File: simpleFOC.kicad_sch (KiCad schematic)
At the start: 20 parts, among them M1 Conn_01x03, M2 Conn_01x03, U6 DRV8313PWP, U7 DRV8313PWP

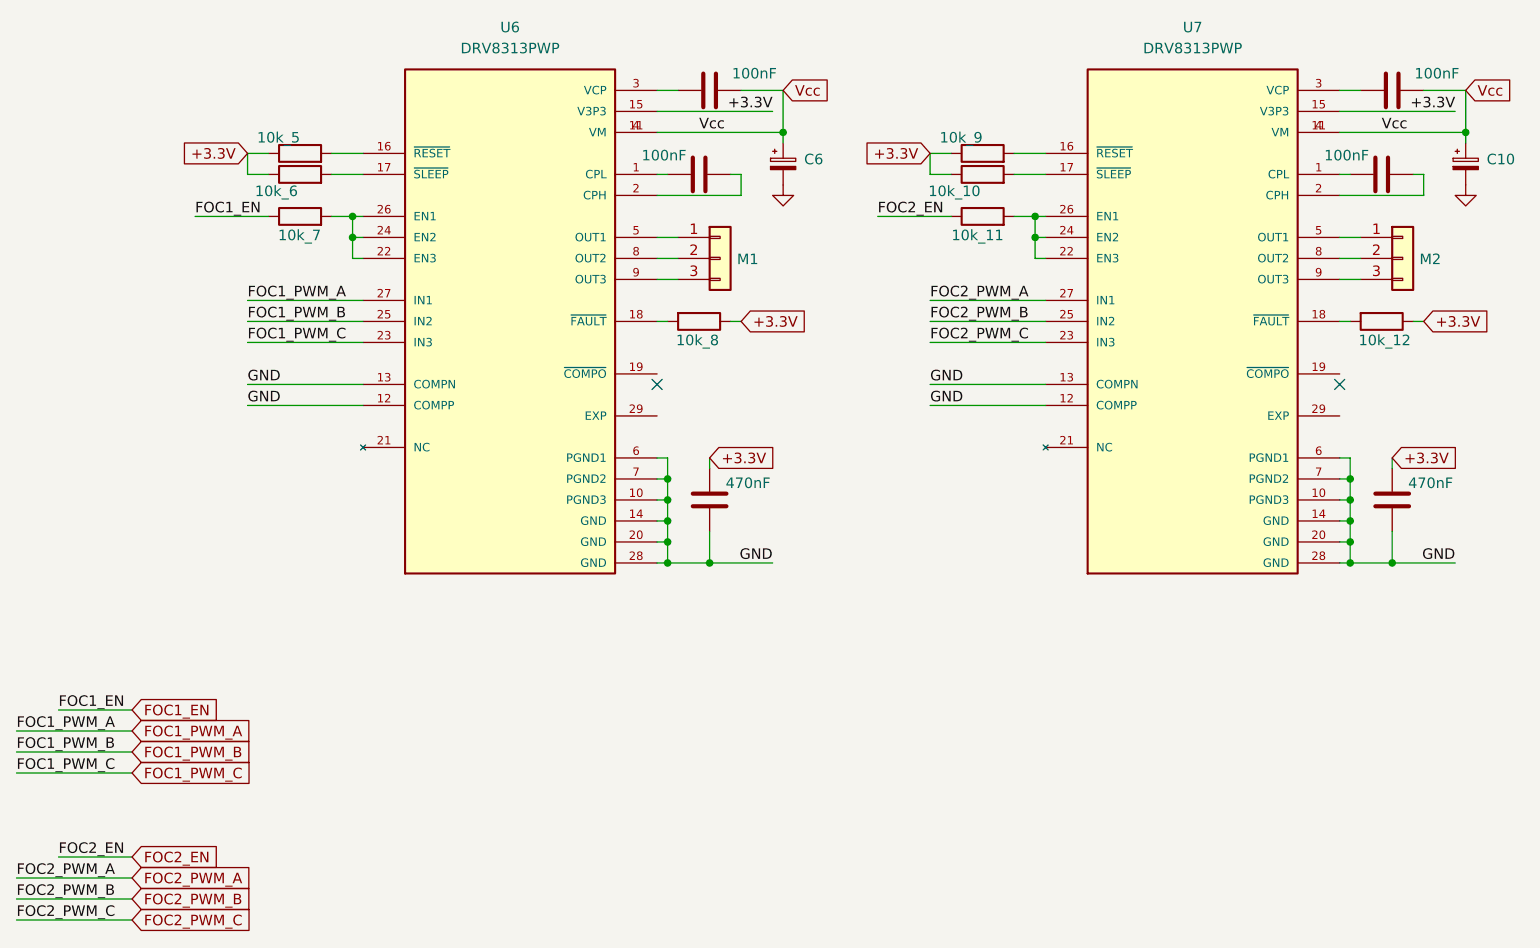
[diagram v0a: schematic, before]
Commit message: added DRV8313
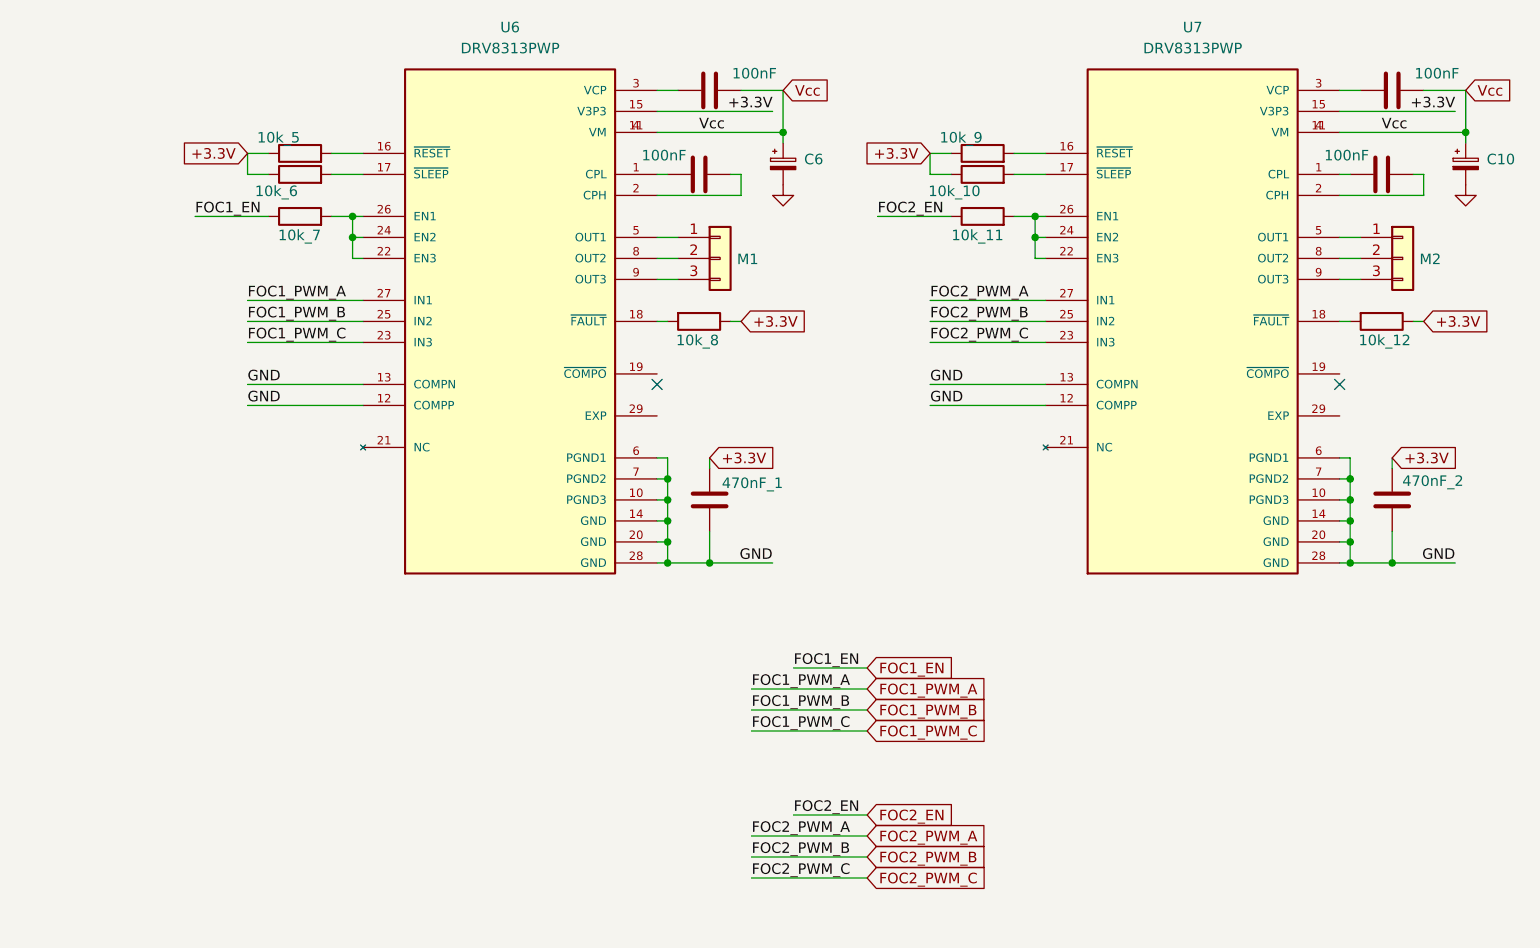
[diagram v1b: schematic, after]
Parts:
- renumbered C5 to 470nF_1, C9 to 470nF_2
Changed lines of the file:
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@@
 	(wire
 		(pts
-			(xy 33.02 154.94) (xy 46.99 154.94)
+			(xy 121.92 149.86) (xy 135.89 149.86)
 		)
 		(stroke
@@
 	(wire
 		(pts
-			(xy 38.1 167.64) (xy 46.99 167.64)
+			(xy 127 162.56) (xy 135.89 162.56)
 		)
 		(stroke
@@
 	(wire
 		(pts
-			(xy 33.02 152.4) (xy 46.99 152.4)
+			(xy 121.92 147.32) (xy 135.89 147.32)
 		)
 		(stroke
@@
 	(wire
 		(pts
-			(xy 33.02 170.18) (xy 46.99 170.18)
+			(xy 121.92 165.1) (xy 135.89 165.1)
 		)
 		(stroke
@@
 	(wire
 		(pts
-			(xy 33.02 157.48) (xy 46.99 157.48)
+			(xy 121.92 152.4) (xy 135.89 152.4)
 		)
 		(stroke
@@
 	(wire
 		(pts
-			(xy 38.1 149.86) (xy 46.99 149.86)
+			(xy 127 144.78) (xy 135.89 144.78)
 		)
 		(stroke
@@
 	(wire
 		(pts
-			(xy 33.02 175.26) (xy 46.99 175.26)
+			(xy 121.92 170.18) (xy 135.89 170.18)
 		)
 		(stroke
@@
 	(wire
 		(pts
-			(xy 33.02 172.72) (xy 46.99 172.72)
+			(xy 121.92 167.64) (xy 135.89 167.64)
 		)
 		(stroke
@@
 	)
 	(label "FOC1_PWM_B"
-		(at 33.02 154.94 0)
+		(at 121.92 149.86 0)
 		(effects
 			(font
@@
 	)
 	(label "FOC2_EN"
-		(at 38.1 167.64 0)
+		(at 127 162.56 0)
 		(effects
 			(font
@@
 	)
 	(label "FOC2_PWM_C"
-		(at 33.02 175.26 0)
+		(at 121.92 170.18 0)
 		(effects
 			(font
@@
 	)
 	(label "FOC2_PWM_A"
-		(at 33.02 170.18 0)
+		(at 121.92 165.1 0)
 		(effects
 			(font
@@
 	)
 	(label "FOC1_PWM_C"
-		(at 33.02 157.48 0)
+		(at 121.92 152.4 0)
 		(effects
 			(font
@@
 	)
 	(label "FOC2_PWM_B"
-		(at 33.02 172.72 0)
+		(at 121.92 167.64 0)
 		(effects
 			(font
@@
 	)
 	(label "FOC1_PWM_A"
-		(at 33.02 152.4 0)
+		(at 121.92 147.32 0)
 		(effects
 			(font
@@
 	)
 	(label "FOC1_EN"
-		(at 38.1 149.86 0)
+		(at 127 144.78 0)
 		(effects
 			(font
@@
 	(global_label "FOC1_PWM_A"
 		(shape input)
-		(at 46.99 152.4 0)
+		(at 135.89 147.32 0)
 		(fields_autoplaced yes)
 		(effects
@@
 		)
 		(property "Intersheetrefs" "${INTERSHEET_REFS}"
-			(at 61.4162 152.4 0)
+			(at 150.3162 147.32 0)
 			(effects
 				(font
@@
 	(global_label "FOC1_PWM_B"
 		(shape input)
-		(at 46.99 154.94 0)
+		(at 135.89 149.86 0)
 		(fields_autoplaced yes)
 		(effects
@@
 		)
 		(property "Intersheetrefs" "${INTERSHEET_REFS}"
-			(at 61.5976 154.94 0)
+			(at 150.4976 149.86 0)
 			(effects
 				(font
@@
 	(global_label "FOC2_PWM_A"
 		(shape input)
-		(at 46.99 170.18 0)
+		(at 135.89 165.1 0)
 		(fields_autoplaced yes)
 		(effects
@@
 		)
 		(property "Intersheetrefs" "${INTERSHEET_REFS}"
-			(at 61.4162 170.18 0)
+			(at 150.3162 165.1 0)
 			(effects
 				(font
@@
 	(global_label "FOC1_EN"
 		(shape input)
-		(at 46.99 149.86 0)
+		(at 135.89 144.78 0)
 		(fields_autoplaced yes)
 		(effects
@@
 		)
 		(property "Intersheetrefs" "${INTERSHEET_REFS}"
-			(at 57.6667 149.86 0)
+			(at 146.5667 144.78 0)
 			(effects
 				(font
@@
 	(global_label "FOC2_EN"
 		(shape input)
-		(at 46.99 167.64 0)
+		(at 135.89 162.56 0)
 		(fields_autoplaced yes)
 		(effects
@@
 		)
 		(property "Intersheetrefs" "${INTERSHEET_REFS}"
-			(at 57.6667 167.64 0)
+			(at 146.5667 162.56 0)
 			(effects
 				(font
@@
 	(global_label "FOC2_PWM_B"
 		(shape input)
-		(at 46.99 172.72 0)
+		(at 135.89 167.64 0)
 		(fields_autoplaced yes)
 		(effects
@@
 		)
 		(property "Intersheetrefs" "${INTERSHEET_REFS}"
-			(at 61.5976 172.72 0)
+			(at 150.4976 167.64 0)
 			(effects
 				(font
@@
 	(global_label "FOC1_PWM_C"
 		(shape input)
-		(at 46.99 157.48 0)
+		(at 135.89 152.4 0)
 		(fields_autoplaced yes)
 		(effects
@@
 		)
 		(property "Intersheetrefs" "${INTERSHEET_REFS}"
-			(at 61.5976 157.48 0)
+			(at 150.4976 152.4 0)
 			(effects
 				(font
@@
 	(global_label "FOC2_PWM_C"
 		(shape input)
-		(at 46.99 175.26 0)
+		(at 135.89 170.18 0)
 		(fields_autoplaced yes)
 		(effects
@@
 		)
 		(property "Intersheetrefs" "${INTERSHEET_REFS}"
-			(at 61.5976 175.26 0)
+			(at 150.4976 170.18 0)
 			(effects
 				(font
@@
 		(on_board yes)
 		(dnp no)
-		(property "Reference" "C5"
-			(at 121.285 127 0)
+		(property "Reference" "470nF_1"
+			(at 125.73 122.428 0)
 			(effects
 				(font
@@
 				)
 				(justify left)
-				(hide yes)
 			)
 		)
@@
 				)
 				(justify left)
+				(hide yes)
 			)
 		)
@@
 			(project "two_motor_driver"
 				(path "/db439bb6-f05c-42b6-bea7-1f689aebc958/d9d208ac-9d68-4acb-92b0-b50eb2d72a1b"
-					(reference "C5")
+					(reference "470nF_1")
 					(unit 1)
 				)
@@
 		(on_board yes)
 		(dnp no)
-		(property "Reference" "C9"
-			(at 203.835 127 0)
+		(property "Reference" "470nF_2"
+			(at 208.026 122.174 0)
 			(effects
 				(font
@@
 				)
 				(justify left)
-				(hide yes)
 			)
 		)
@@
 				)
 				(justify left)
+				(hide yes)
 			)
 		)
@@
 			(project "two_motor_driver"
 				(path "/db439bb6-f05c-42b6-bea7-1f689aebc958/d9d208ac-9d68-4acb-92b0-b50eb2d72a1b"
-					(reference "C9")
+					(reference "470nF_2")
 					(unit 1)
 				)
